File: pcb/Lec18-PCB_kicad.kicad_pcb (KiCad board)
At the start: 2 copper layers, 65 x 56 mm, 5 parts, among them P1 Conn_02x20_Odd_Even

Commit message: Fork Lift
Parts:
- added J1: HBRIDGE_LEFT, Connector_PinSocket_2.54mm:PinSocket_1x08_P2.54mm_Vertical, F.Cu at (85.7, 76.1)
- added J2: HBRIDGE_RIGHT, Connector_PinSocket_2.54mm:PinSocket_1x08_P2.54mm_Vertical, F.Cu at (85.7, 61.1)
- added J3: MOTOR_A, Connector_PinHeader_2.54mm:PinHeader_1x02_P2.54mm_Vertical, F.Cu at (74.0, 63.0)
- added J4: MOTOR_B, Connector_PinHeader_2.54mm:PinHeader_1x02_P2.54mm_Vertical, F.Cu at (74.0, 91.0)
- added J5: SERVO_1, Connector_PinHeader_2.54mm:PinHeader_1x03_P2.54mm_Vertical, F.Cu at (78.1, 72.5)
- added J6: SERVO_2, Connector_PinHeader_2.54mm:PinHeader_1x03_P2.54mm_Vertical, F.Cu at (116.0, 71.9)
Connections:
- P1 pad 11: /GPIO17(GEN0) -> /AI1
- P1 pad 13: /GPIO27(GEN2) -> /AI2
- P1 pad 15: /GPIO22(GEN3) -> /BI1
- P1 pad 16: /GPIO23(GEN4) -> /BI2
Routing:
- net GND: track 0.00 -> 129.9 mm
- net +5V: track 0.00 -> 92.9 mm
- net /GPIO13(PWM1): track 0.00 -> 59.2 mm
- net /B01: track 0.00 -> 33.2 mm
- net /B02: track 0.00 -> 29.6 mm
- net /A02: track 0.00 -> 28.4 mm
- net /GPIO19(SPI1_MISO): track 0.00 -> 27.7 mm
- net /A01: track 0.00 -> 24.8 mm
- net /GPIO12(PWM0): track 0.00 -> 23.1 mm
- net +3V3: track 0.00 -> 21.3 mm
- net /BI2: track 0.00 -> 18.2 mm
- net /GPIO18(GEN1)(PWM0): track 0.00 -> 17.1 mm
- net /BI1: track 0.00 -> 17.0 mm
- net /AI1: track 0.00 -> 16.9 mm
- net /GPIO24(GEN5): track 0.00 -> 14.8 mm
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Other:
- outline, holes or cut-outs redrawn
- board text added: "A01"
- board text added: "A02"
- board text added: "AI1"
- board text added: "AI2"
- board text added: "Anita Huang & Gabriel Yuen"
- board text added: "B01"
- board text added: "B02"
- board text added: "BI1"
- board text added: "BI2"
- board text added: "GND"
- board text added: "H-Bridge"
- board text added: "MOTOR A"
- board text added: "MOTOR B"
- board text added: "PWMA"
- board text added: "PWMB"
- board text added: "STBY"
- board text added: "Servo1"
- board text added: "Servo2"
- board text added: "VCC"
- board text added: "VM"

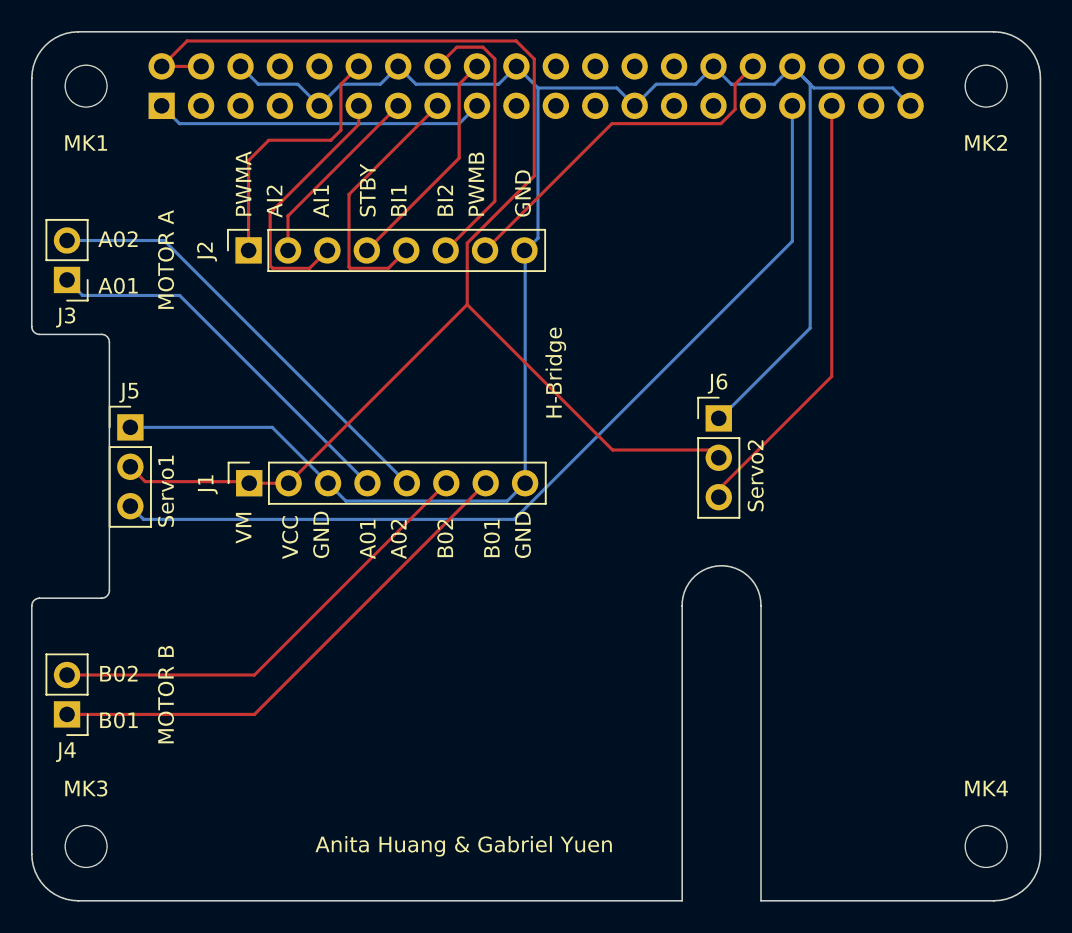
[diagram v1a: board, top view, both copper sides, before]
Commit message: Integrated Second Socket
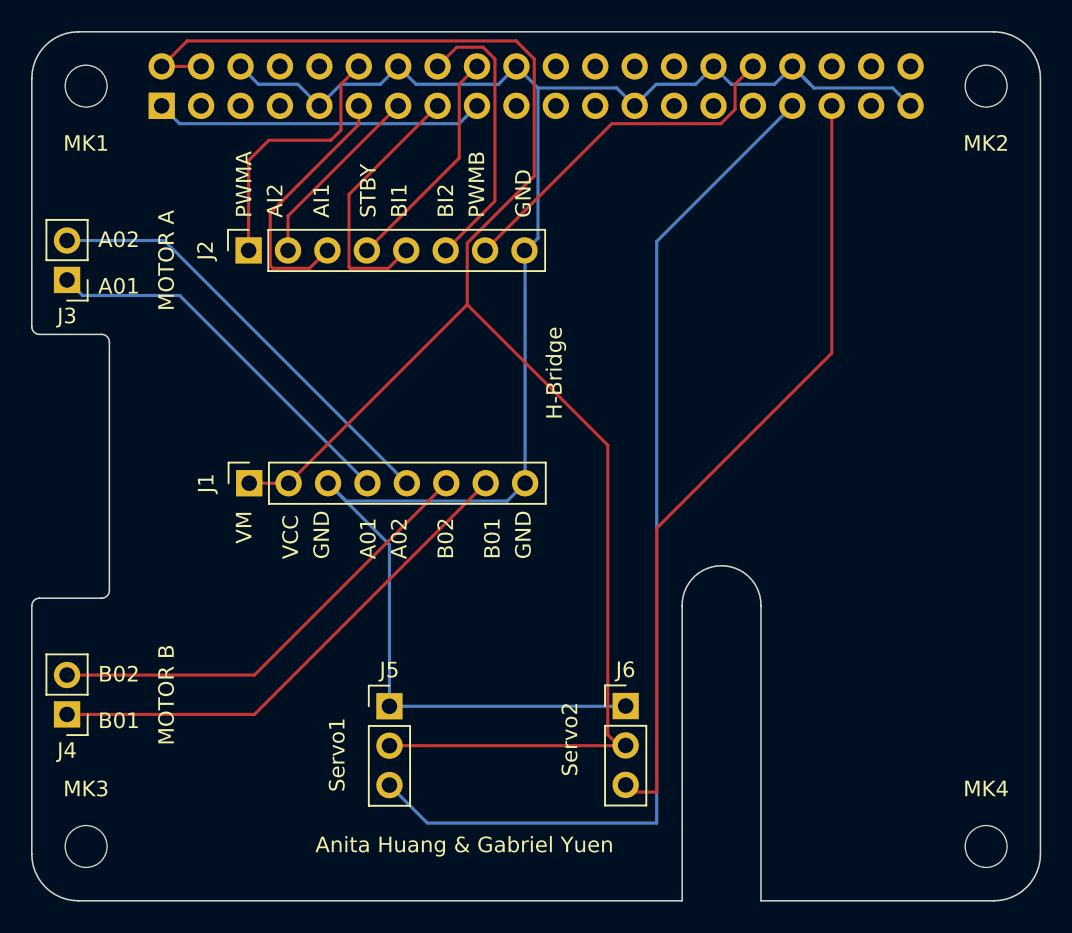
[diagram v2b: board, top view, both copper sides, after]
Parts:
- moved J5 24.5 mm to (94.8, 90.5)
- moved J6 19.5 mm to (110.0, 90.5)
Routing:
- net /GPIO19(SPI1_MISO): track 27.7 -> 50.9 mm
- net +5V: track 92.9 -> 112.8 mm
- net /GPIO13(PWM1): track 59.2 -> 68.1 mm
- net GND: track 129.9 -> 122.7 mm
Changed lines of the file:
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@@
 		(tags "Through hole pin header THT 1x02 2.54mm single row")
 		(property "Reference" "J3"
-			(at 0 -2.33 360)
+			(at 0 -2.33 0)
 			(layer "F.SilkS")
 			(effects
@@
 		)
 		(property "Value" "MOTOR_A"
-			(at 0 4.87 360)
+			(at 0 4.87 0)
 			(layer "F.Fab")
 			(effects
@@
 	(footprint "Connector_PinHeader_2.54mm:PinHeader_1x03_P2.54mm_Vertical"
 		(layer "F.Cu")
-		(at 116 71.92)
+		(at 110 90.46)
 		(descr "Through hole straight pin header, 1x03, 2.54mm pitch, single row")
 		(tags "Through hole pin header THT 1x03 2.54mm single row")
@@
 		(tags "Through hole pin header THT 1x02 2.54mm single row")
 		(property "Reference" "J4"
-			(at 0 -2.33 360)
+			(at 0 -2.33 0)
 			(layer "F.SilkS")
 			(effects
@@
 		)
 		(property "Value" "MOTOR_B"
-			(at 0 4.87 360)
+			(at 0 4.87 0)
 			(layer "F.Fab")
 			(effects
@@
 	(footprint "Connector_PinHeader_2.54mm:PinHeader_1x03_P2.54mm_Vertical"
 		(layer "F.Cu")
-		(at 78.08 72.5)
+		(at 94.777505 90.475)
 		(descr "Through hole straight pin header, 1x03, 2.54mm pitch, single row")
 		(tags "Through hole pin header THT 1x03 2.54mm single row")
@@
 	)
 	(gr_text "Servo1"
-		(at 81 79 90)
+		(at 92 96 90)
 		(layer "F.SilkS")
 		(effects
@@
 	)
 	(gr_text "Servo2"
-		(at 119 78 90)
+		(at 107 95 90)
 		(layer "F.SilkS")
 		(effects
@@
 	)
 	(segment
+		(start 108.85 73.65)
+		(end 99.79 64.59)
+		(width 0.2)
+		(layer "F.Cu")
+		(net 2)
+	)
+	(segment
 		(start 82.64 49.24)
 		(end 80.1 49.24)
@@
 	)
 	(segment
-		(start 80.1 49.24)
-		(end 81.74 47.6)
+		(start 108.85 92.31)
+		(end 108.85 73.65)
 		(width 0.2)
 		(layer "F.Cu")
@@
 	)
 	(segment
-		(start 99.79 64.59)
-		(end 88.28 76.1)
+		(start 80.1 49.24)
+		(end 81.74 47.6)
 		(width 0.2)
 		(layer "F.Cu")
@@
 	)
 	(segment
-		(start 102.946346 47.6)
-		(end 104.11 48.763654)
+		(start 99.79 64.59)
+		(end 88.28 76.1)
 		(width 0.2)
 		(layer "F.Cu")
@@
 	)
 	(segment
-		(start 116 73.96)
-		(end 109.16 73.96)
+		(start 94.777505 93.015)
+		(end 109.985 93.015)
 		(width 0.2)
 		(layer "F.Cu")
@@
 	)
 	(segment
-		(start 99.79 60.623654)
-		(end 99.79 64.59)
+		(start 110 93.46)
+		(end 108.85 92.31)
 		(width 0.2)
 		(layer "F.Cu")
@@
 	)
 	(segment
-		(start 85.74 76.1)
-		(end 88.28 76.1)
+		(start 102.946346 47.6)
+		(end 104.11 48.763654)
 		(width 0.2)
 		(layer "F.Cu")
@@
 	)
 	(segment
-		(start 86 76)
-		(end 79.04 76)
+		(start 99.79 60.623654)
+		(end 99.79 64.59)
 		(width 0.2)
 		(layer "F.Cu")
@@
 	)
 	(segment
-		(start 79.04 76)
-		(end 78.08 75.04)
+		(start 85.74 76.1)
+		(end 88.28 76.1)
 		(width 0.2)
 		(layer "F.Cu")
@@
 	)
 	(segment
-		(start 109.16 73.96)
-		(end 99.79 64.59)
+		(start 109.985 93.015)
+		(end 110 93)
 		(width 0.2)
 		(layer "F.Cu")
@@
 	)
 	(segment
+		(start 109.985 90.475)
+		(end 110 90.46)
+		(width 0.2)
+		(layer "B.Cu")
+		(net 3)
+	)
+	(segment
 		(start 120.74 49.24)
 		(end 119.59 50.39)
@@
 	)
 	(segment
-		(start 86.33 50.39)
-		(end 85.18 49.24)
-		(width 0.2)
-		(layer "B.Cu")
-		(net 3)
-	)
-	(segment
-		(start 116 72)
-		(end 121.89 66.11)
+		(start 94.777505 90.475)
+		(end 109.985 90.475)
 		(width 0.2)
 		(layer "B.Cu")
@@
 	)
 	(segment
-		(start 87.22 72.5)
-		(end 90.82 76.1)
+		(start 86.33 50.39)
+		(end 85.18 49.24)
 		(width 0.2)
 		(layer "B.Cu")
@@
 	)
 	(segment
-		(start 78.08 72.5)
-		(end 87.22 72.5)
-		(width 0.2)
-		(layer "B.Cu")
-		(net 3)
-	)
-	(segment
 		(start 104.35 50.63)
 		(end 102.96 49.24)
@@
 	)
 	(segment
-		(start 121.89 66.11)
-		(end 121.89 50.39)
+		(start 116.81 50.39)
+		(end 115.66 49.24)
 		(width 0.2)
 		(layer "B.Cu")
@@
 	)
 	(segment
-		(start 116.81 50.39)
-		(end 115.66 49.24)
+		(start 94.777505 90.475)
+		(end 94.777505 80.057505)
 		(width 0.2)
 		(layer "B.Cu")
@@
 	)
 	(segment
-		(start 116 71.92)
-		(end 116 72)
+		(start 102.96 49.24)
+		(end 101.81 50.39)
 		(width 0.2)
 		(layer "B.Cu")
@@
 	)
 	(segment
-		(start 102.96 49.24)
-		(end 101.81 50.39)
+		(start 94.19 50.39)
+		(end 91.65 50.39)
 		(width 0.2)
 		(layer "B.Cu")
@@
 	)
 	(segment
-		(start 94.19 50.39)
-		(end 91.65 50.39)
+		(start 94.777505 80.057505)
+		(end 90.82 76.1)
 		(width 0.2)
 		(layer "B.Cu")
@@
 	)
 	(segment
-		(start 120.74 60.506346)
+		(start 112 60.52)
 		(end 120.74 51.78)
 		(width 0.2)
@@
 	)
 	(segment
-		(start 78.93 78.43)
-		(end 102.816346 78.43)
+		(start 97.222505 98)
+		(end 112 98)
 		(width 0.2)
 		(layer "B.Cu")
@@
 	)
 	(segment
-		(start 78.08 77.58)
-		(end 78.93 78.43)
+		(start 112 98)
+		(end 112 60.52)
 		(width 0.2)
 		(layer "B.Cu")
@@
 	)
 	(segment
-		(start 102.816346 78.43)
-		(end 120.74 60.506346)
+		(start 94.777505 95.555)
+		(end 97.222505 98)
 		(width 0.2)
 		(layer "B.Cu")
@@
 	)
 	(segment
-		(start 116 76.5)
-		(end 123.28 69.22)
+		(start 112 96)
+		(end 112 79)
+		(width 0.2)
+		(layer "F.Cu")
+		(net 24)
+	)
+	(segment
+		(start 112 79)
+		(end 123.28 67.72)
 		(width 0.2)
 		(layer "F.Cu")
@@
 	)
 	(segment
-		(start 123.28 69.22)
+		(start 123.28 67.72)
 		(end 123.28 51.78)
 		(width 0.2)
 		(layer "F.Cu")
+		(net 24)
+	)
+	(segment
+		(start 110 96)
+		(end 112 96)
+		(width 0.2)
+		(layer "F.Cu")
